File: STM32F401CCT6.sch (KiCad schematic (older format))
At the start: 43 parts, among them J1 USB_OTG, J2 Conn_02x03_Odd_Even, J3 Conn_01x20_des, J4 Conn_01x05_desc, J5 Conn_01x20, SW1 SW_Push, U1 MIC5219-3.3, U2 STM32F401CCT6, U3 USBLC6-2SC6, Y1 32.786K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

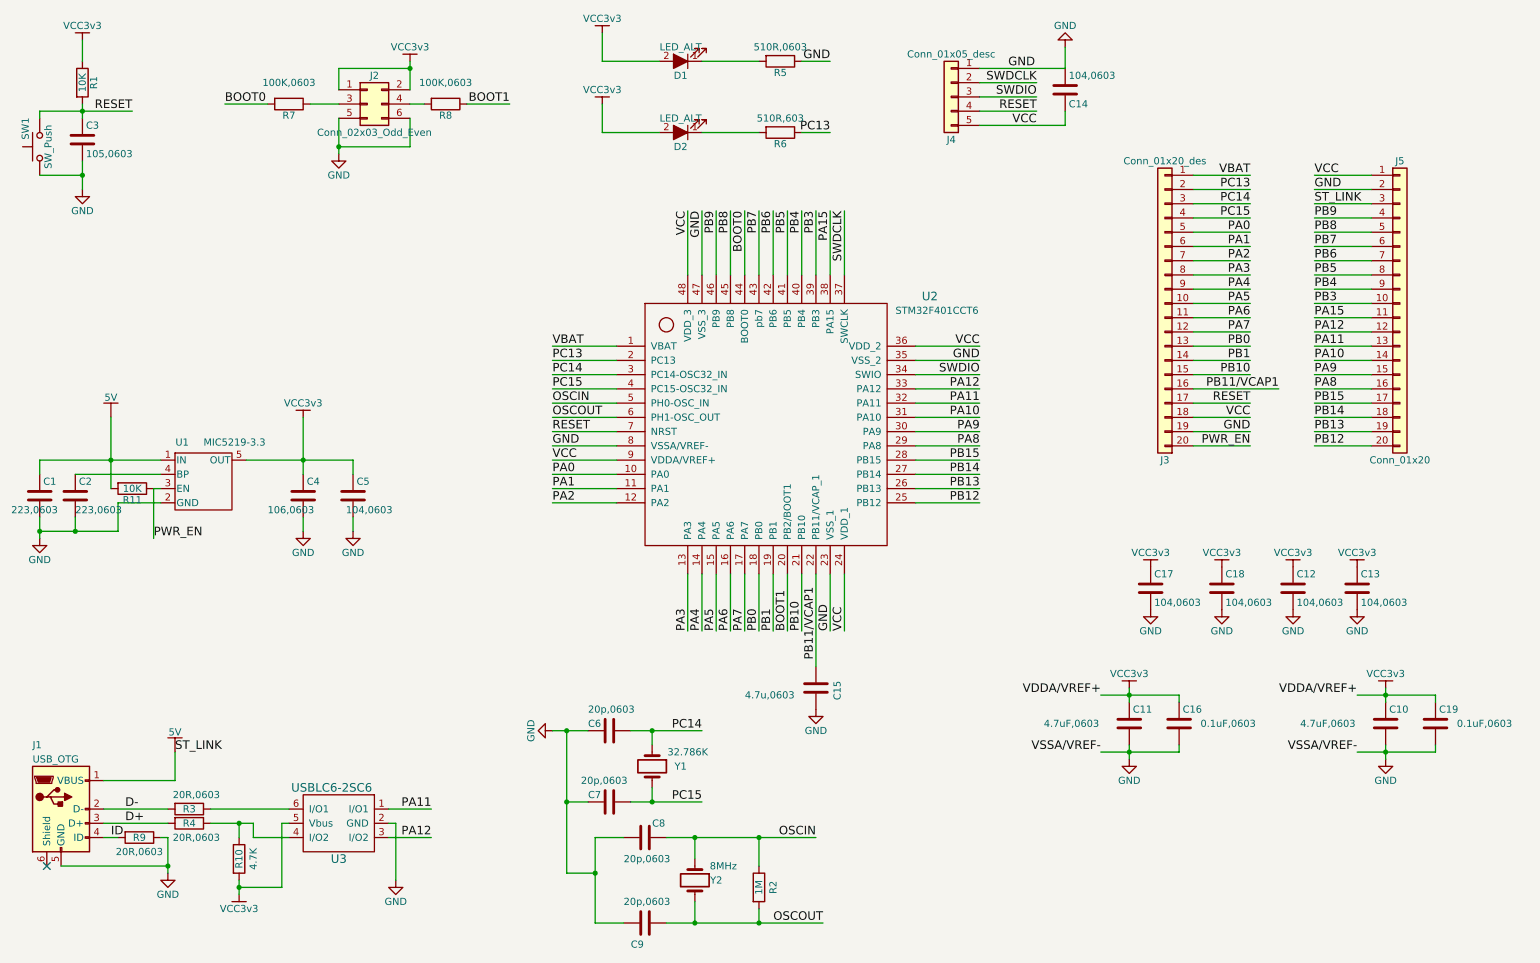
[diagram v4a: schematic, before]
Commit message: Renamed VCC to VDD
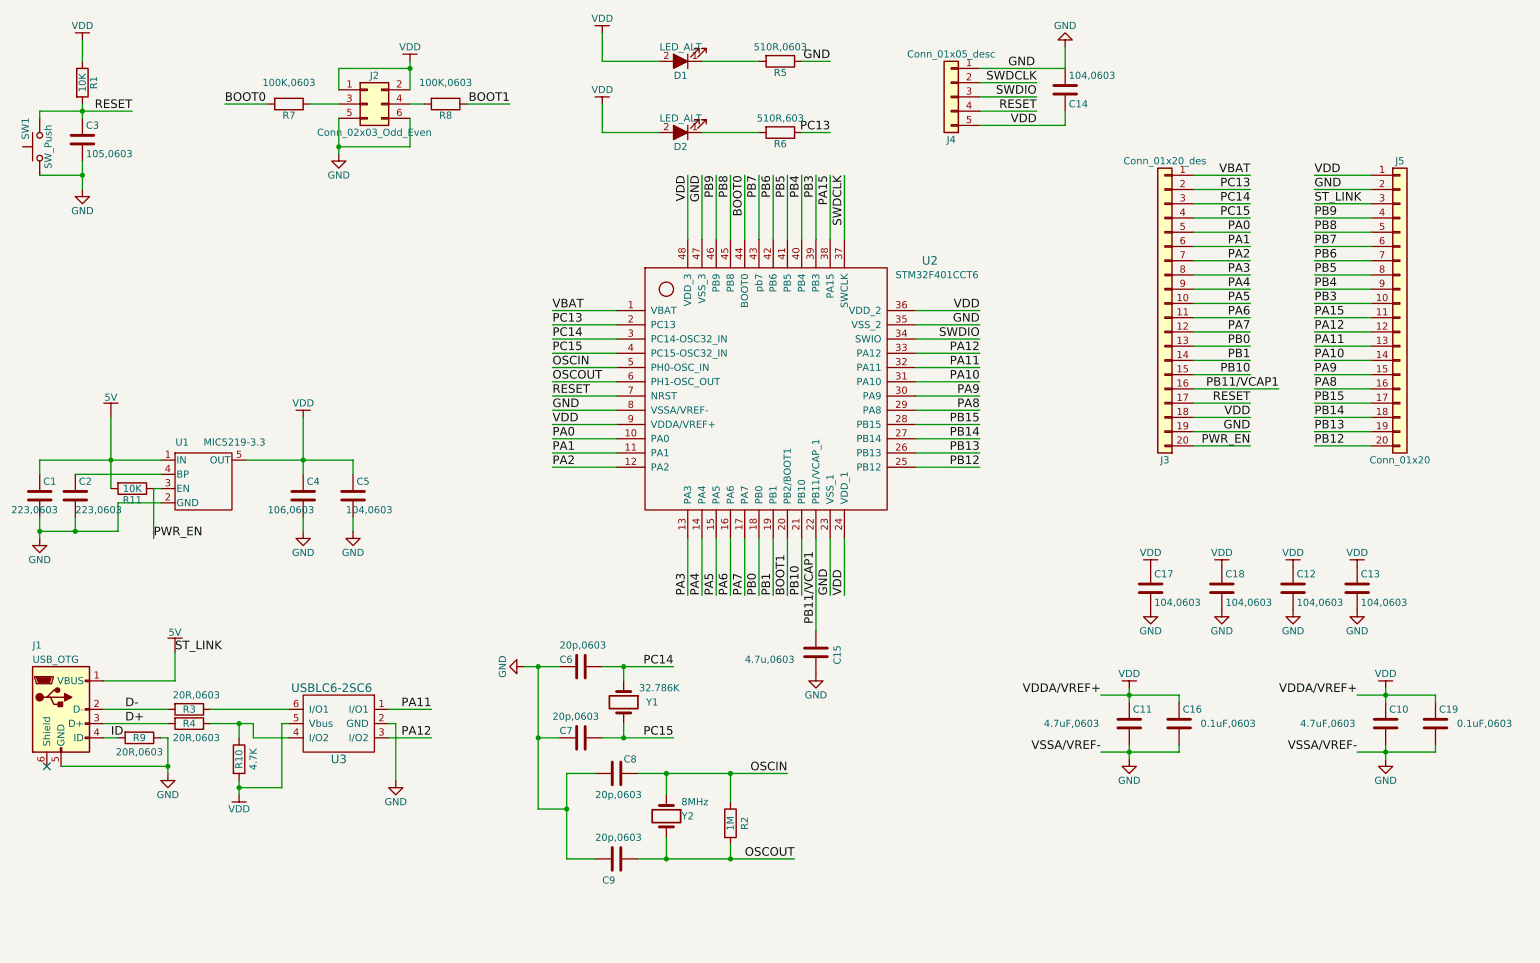
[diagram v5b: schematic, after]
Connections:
- net VCC: no longer C14.1, J3.18 (Pin_18), J4.5 (Pin_5), J5.1 (Pin_1), U2.24 (VDD_1), U2.36 (VDD_2), U2.48 (VDD_3), U2.9 (VDDA/VREF+)
- new net VDD: C14.1, J3.18 (Pin_18), J4.5 (Pin_5), J5.1 (Pin_1), U2.24 (VDD_1), U2.36 (VDD_2), U2.48 (VDD_3), U2.9 (VDDA/VREF+)
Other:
- moved on the sheet: C15, C6, C7, C8, C9, J1, R10, R2, R3, R4, R9, U2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
